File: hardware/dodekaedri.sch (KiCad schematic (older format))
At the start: 0 parts

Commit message: Added initial schematic for frequency synthesizer
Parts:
- added C? (x3): C_Small, symbol C_Small
- added C? (x2): 1µF, symbol C_Small
- added OSC?: TCXO 26MHz, symbol TCXO
- added R? (x2): 10k, symbol R
- added U?: SI5351A, symbol SI5351A
- added U?: LDO, symbol LDO
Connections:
- new net: C?.1, U?.2 (XA)
- new net: R?.2, U?.4 (SCL)
- new net: R?.2, U?.5 (SDA)
- new net: C?.2, OSC?.4 (OUTPUT)
- new net: C?.1, OSC?.6 (VDD), U?.5 (Vout)
- new net +Vlogic: C?.1, C?.1, C?.1, R?.1, R?.1, U?.1 (VDD), U?.1 (Vin), U?.7 (VDDO)
- new net GND: C?.2, C?.2, C?.2, C?.2, OSC?.1 (GND/ENA), OSC?.2 (N.C.), OSC?.3 (GND), U?.2 (GND), U?.3 (EN), U?.8 (GND)
- no-connect marks 0 -> 1

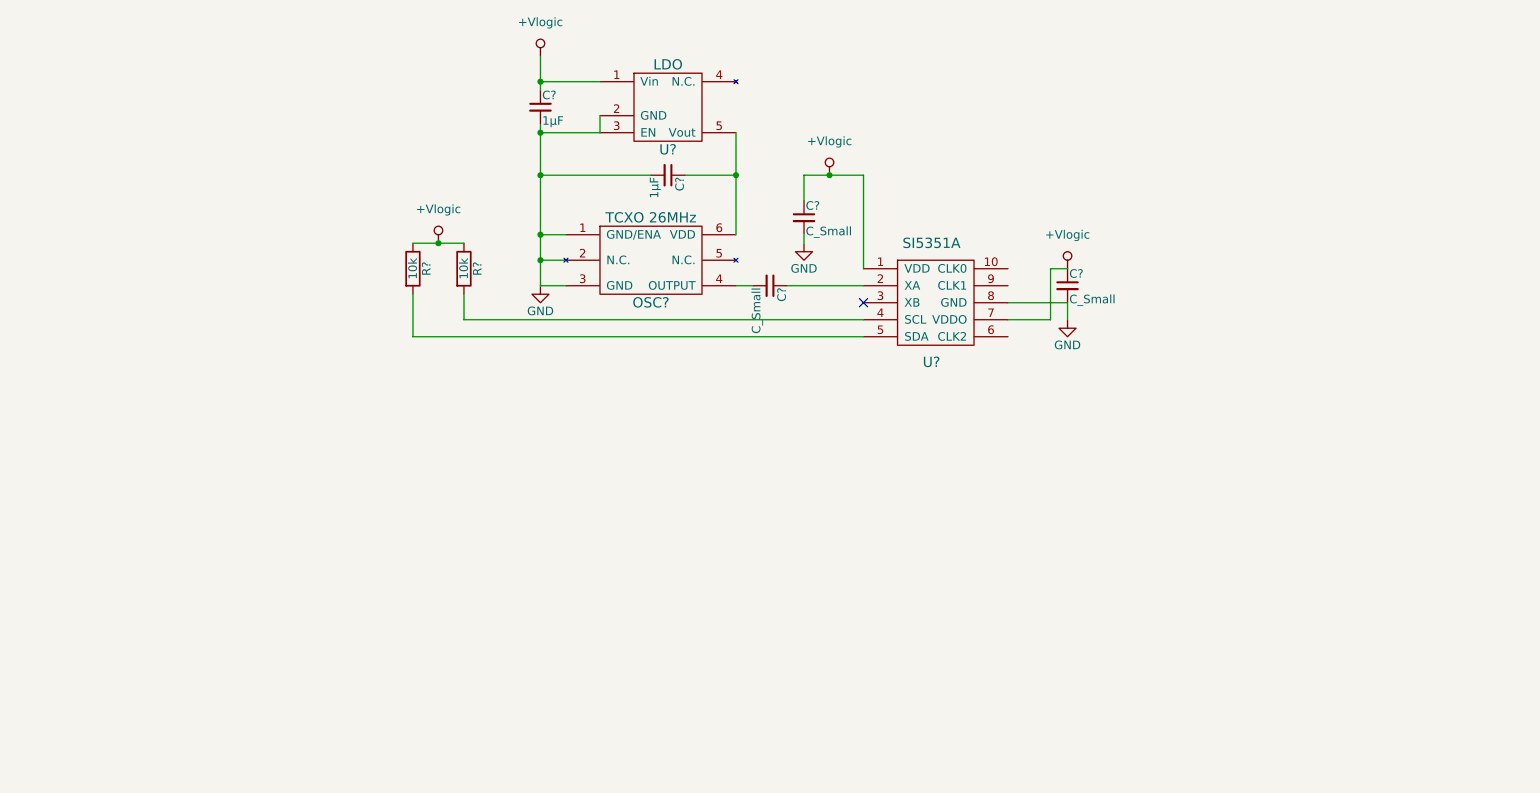
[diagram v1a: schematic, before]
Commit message: Added antenna+SWR+antenna switch schematic block
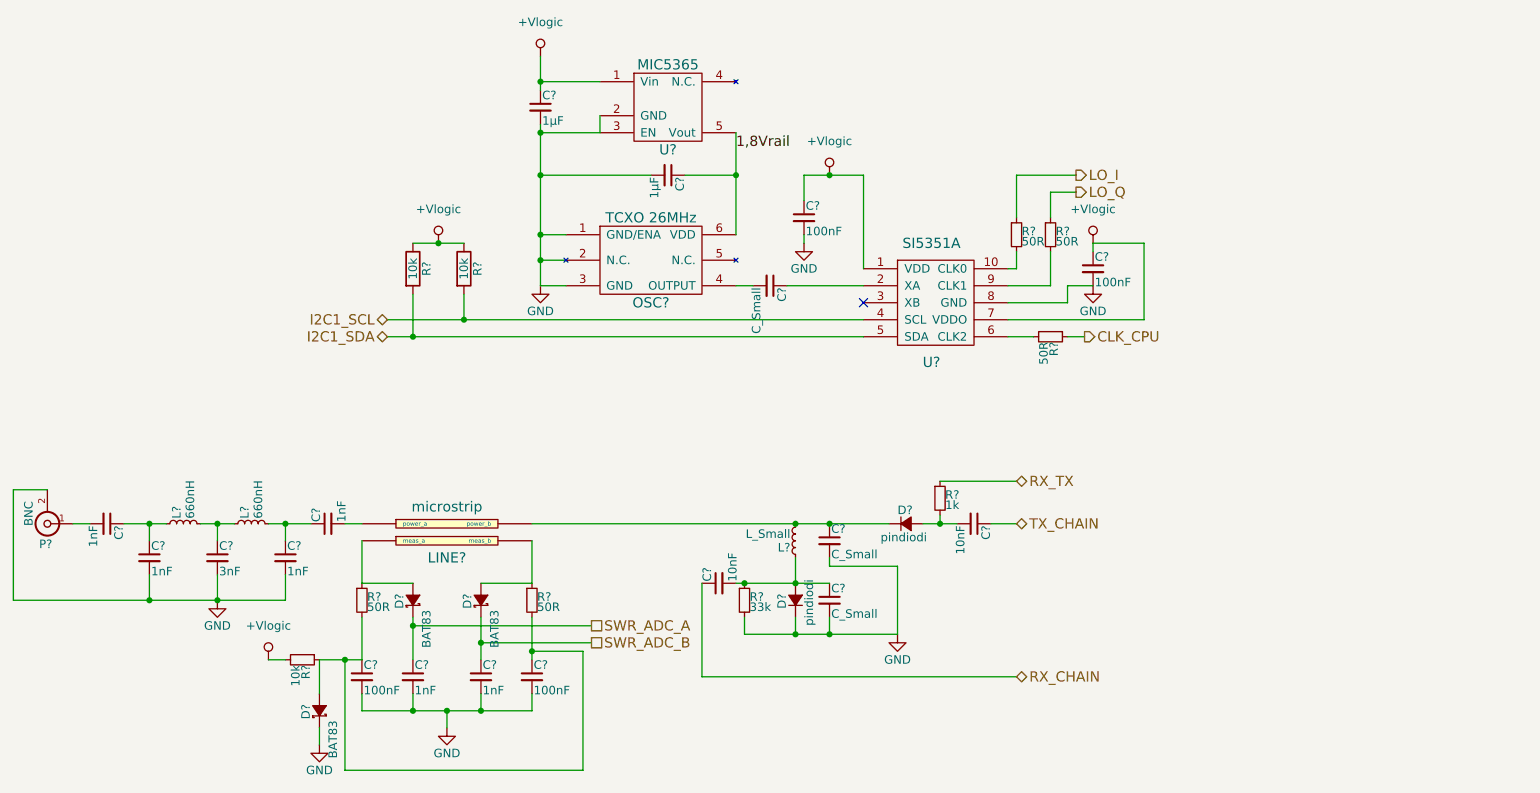
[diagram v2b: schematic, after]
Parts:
- added C? (x6): 1nF, symbol C_Small
- added C?: 3nF, symbol C_Small
- added C? (x2): 100nF, symbol C_Small
- added C? (x2): C_Small, symbol C_Small
- added C? (x2): 10nF, symbol C_Small
- added D? (x3): BAT83, symbol D_Schottky_Small
- added D? (x2): pindiodi, symbol D_Small
- added L? (x2): 660nH, symbol L_Small
- added L?: L_Small, symbol L_Small
- added LINE?: microstrip, symbol microstrip
- added P?: BNC, symbol BNC
- added R? (x5): 50R, symbol R_Small
- added R?: 10k, symbol R_Small
- added R?: 33k, symbol R_Small
- added R?: 1k, symbol R_Small
- C? (x2): value C_Small -> 100nF
- U?: value LDO -> MIC5365
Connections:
- net +Vlogic: now also R?.2
- net GND: now also C?.2, C?.2, C?.2, C?.2, C?.2, C?.2, C?.2, C?.2, C?.2, D?.1 (K), D?.1 (K), P?.2 (Ext), R?.2
- net at U?.10 (CLK0): now also R?.2
- net I2C1_SCL: now reaches R?.2, U?.4 (SCL)
- net I2C1_SDA: now reaches R?.2, U?.5 (SDA)
- net at U?.6 (CLK2): now also R?.2
- net at U?.9 (CLK1): now also R?.2
- net 1,8Vrail: now reaches C?.1, OSC?.6 (VDD), U?.5 (Vout)
- new net: C?.2, P?.1 (In)
- new net: C?.1, C?.1, L?.1
- new net: C?.1, L?.1, L?.2
- new net: C?.1, C?.1, L?.2
- new net: C?.2, LINE?.~ (power_b)
- new net: D?.2 (A), LINE?.~ (power_b), R?.1 (x2)
- new net: C?.1, D?.1 (K), L?.2, LINE?.~ (power_b)
- new net: C?.1, C?.1, D?.2 (A), R?.1, R?.2, R?.2
- new net: C?.1, C?.2, D?.2 (A), L?.1, R?.1
- new net: C?.2, D?.2 (A), R?.2
- new net CLK_CPU: R?.1
- new net LO_I: R?.1
- new net LO_Q: R?.1
- new net RX_CHAIN: C?.1
- new net RX_TX: R?.1
- new net SWR_ADC_A: C?.1, D?.1 (K)
- new net SWR_ADC_B: C?.1, D?.1 (K)
- new net TX_CHAIN: C?.1
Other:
- moved on the sheet: C?

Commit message: Converted schematic into hierarchial one to maintain clarity and to fit whole schematic somewhere
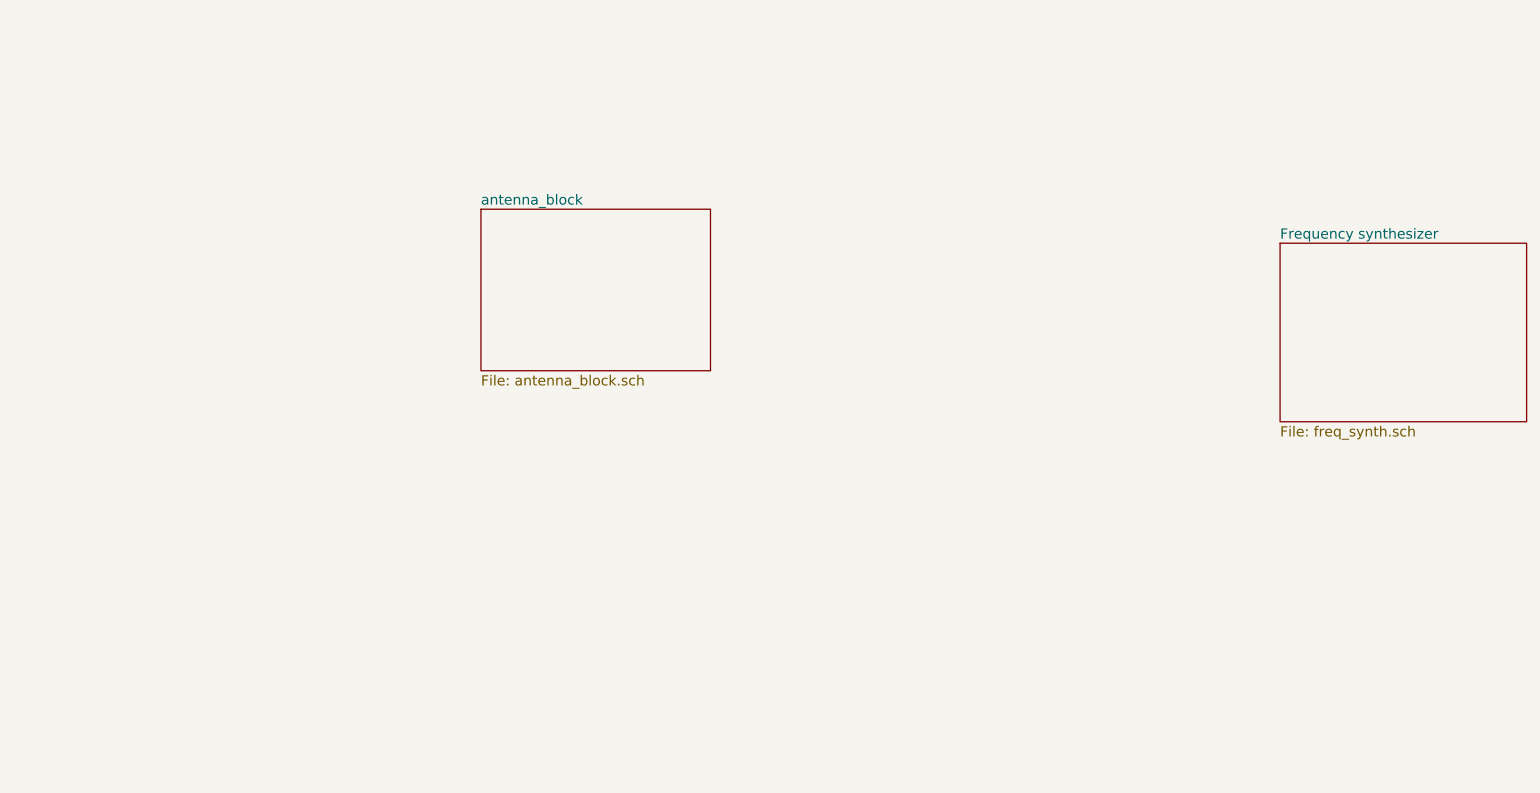
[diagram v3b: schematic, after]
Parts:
- removed C? (x4): 100nF, symbol C_Small
- removed C? (x3): C_Small, symbol C_Small
- removed C? (x2): 1µF, symbol C_Small
- removed C? (x6): 1nF, symbol C_Small
- removed C?: 3nF, symbol C_Small
- removed C? (x2): 10nF, symbol C_Small
- removed D? (x3): BAT83, symbol D_Schottky_Small
- removed D? (x2): pindiodi, symbol D_Small
- removed L? (x2): 660nH, symbol L_Small
- removed L?: L_Small, symbol L_Small
- removed LINE?: microstrip, symbol microstrip
- removed OSC?: TCXO 26MHz, symbol TCXO
- removed P?: BNC, symbol BNC
- removed R? (x2): 10k, symbol R
- removed R? (x5): 50R, symbol R_Small
- removed R?: 10k, symbol R_Small
- removed R?: 33k, symbol R_Small
- removed R?: 1k, symbol R_Small
- removed U?: SI5351A, symbol SI5351A
- removed U?: MIC5365, symbol LDO
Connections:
- no-connect marks 1 -> 0
